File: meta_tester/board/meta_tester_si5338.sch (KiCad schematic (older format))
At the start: 0 parts

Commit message: Adding OPAMP
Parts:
- added C? (x4): CAP_0603, SM0603, symbol CAP_0603
- added C? (x4): CAP_0805, SM0805, symbol CAP_0805
- added P?: USB_OTG, symbol USB_OTG
- added U? (x2): TCA0372BDW-SOIC16, symbol TCA0372BDW-SOIC16
- added U?: MAX5713/4/5-TSSOP14, symbol MAX5713/4/5-TSSOP14
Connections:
- net labels added: +3.3V, +5V, CLR_DAC, CS_DAC, DAC0, DAC1, DAC2, DAC3, GND, MOSI_DAC, SCK_DAC, VddO0, VddO1, VddO2, VddO3
- wire segments 0 -> 85
- no-connect marks 0 -> 3

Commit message: starting layout
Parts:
- removed P?: USB_OTG, symbol USB_OTG
- added C101, C102: 100n, General_SMD:SM0805, symbol CAP_0805
- added C103, C107, C117, C118: 10p, General_SMD:SM0603, symbol CAP_0603
- added C113, C114, C115, C116, C120, C123, C130: 1u, General_SMD:SM0805, symbol CAP_0805
- added C119, C122, C125, C127: CAP_0603, General_SMD:SM0603, symbol CAP_0603
- added C121, C124, C126, C129: CAP_0805, General_SMD:SM0805, symbol CAP_0805
- added C128: 10n, General_SMD:SM0603, symbol CAP_0603
- added J101, J102, J103, J104, J105, J106, J107, J108: SMA_PCB, Connectors_RF:Border_Antenna, symbol SMA_PCB
- added L101, L102, L103: IND_0603, General_SMD:SM0603, symbol IND_0603
- added P101: USB_OTG, Connectors:USB_Mini-B, symbol USB_OTG
- added R101, R102, R103, R104: 1M, General_SMD:SM0603, symbol RES_0603
- added U103: STM32F103TB-QFN36, QFN:QFN36_6x6_0.5mm, symbol STM32F103TB-QFN36
- added U105: CH340T-SSOP20, SSOP:SSOP-20, symbol CH340T-SSOP20
- added U106: REG113-XX-SOT23, SOT:SOT-236-095mm, symbol REG113-XX-SOT23
- added X101: 8MHz, Xtal_SMD:xtal_3.2x2.5, symbol SMD_XTAL_small
- added X102: 12MHz, Xtal_SMD:xtal_3.2x2.5, symbol SMD_XTAL_small
- C104, C106, C109, C111: renamed from C?; footprint SM0603 -> General_SMD:SM0603
- C105, C108, C110, C112: renamed from C?; footprint SM0805 -> General_SMD:SM0805
- U101: renamed from U?; footprint (none) -> SSOP:SSOP14
- U102, U104: renamed from U?; footprint (none) -> SOIC:SOIC-16-10.3x7.5
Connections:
- net labels added: 5338_INT, D_N, D_P, PSU01, PSU23, SCL, SDA, US1_CTS, US1_RTS, US1_RX, US1_TX
- wire segments 85 -> 240
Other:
- note added: "3.3V"

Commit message: reversed CTS/RTS
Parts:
- P101: symbol USB_OTG -> USB_OTG-RESCUE-meta_tester_si5338
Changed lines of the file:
@@
 $EndComp
 $Comp
-L USB_OTG P101
+L USB_OTG-RESCUE-meta_tester_si5338 P101
 U 1 1 58AEF4E6
 P 8825 1450
@@
 Text Label 8125 1350 2    25   ~ 0
 US1_RX
+Text Label 7100 1700 0    25   ~ 0
+US1_RTS
 Text Label 7100 1450 0    25   ~ 0
-US1_RTS
-Text Label 7100 1700 0    25   ~ 0
 US1_CTS
 Wire Wire Line

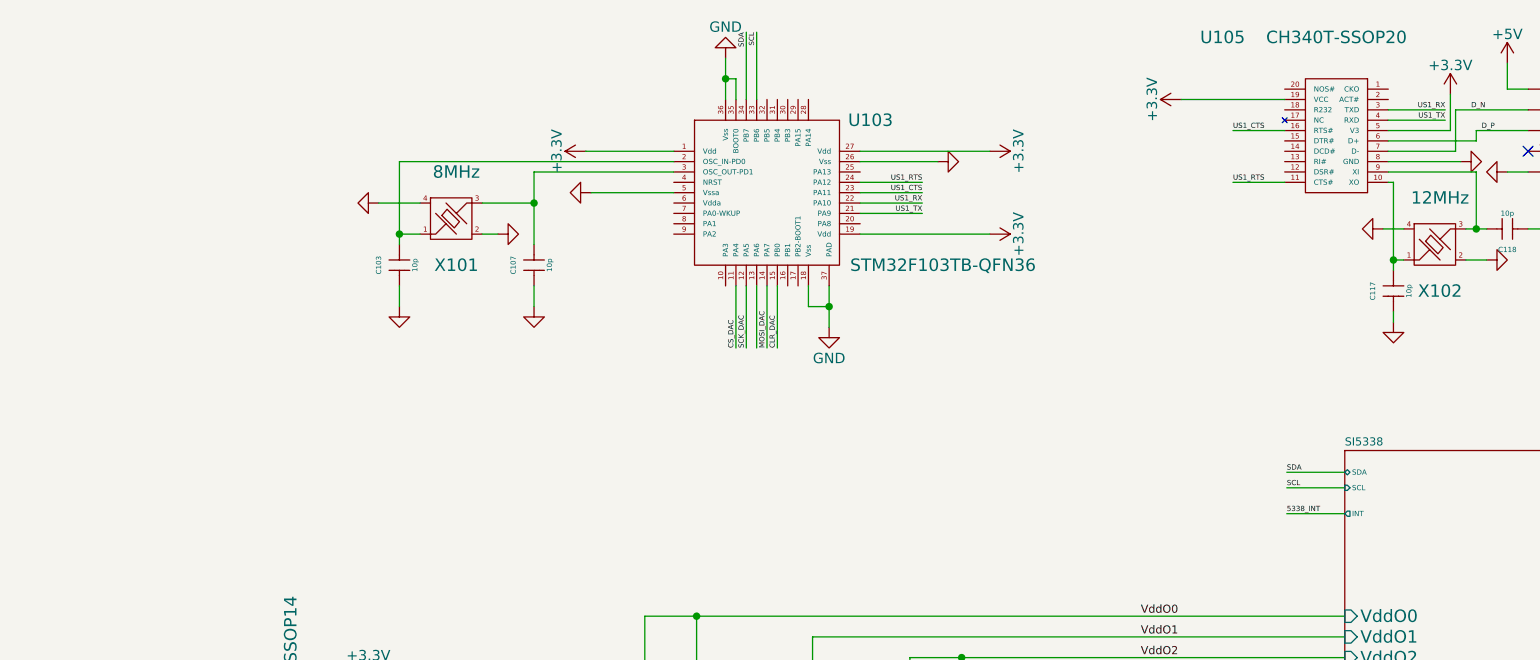
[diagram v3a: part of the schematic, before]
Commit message: adding jtag connector
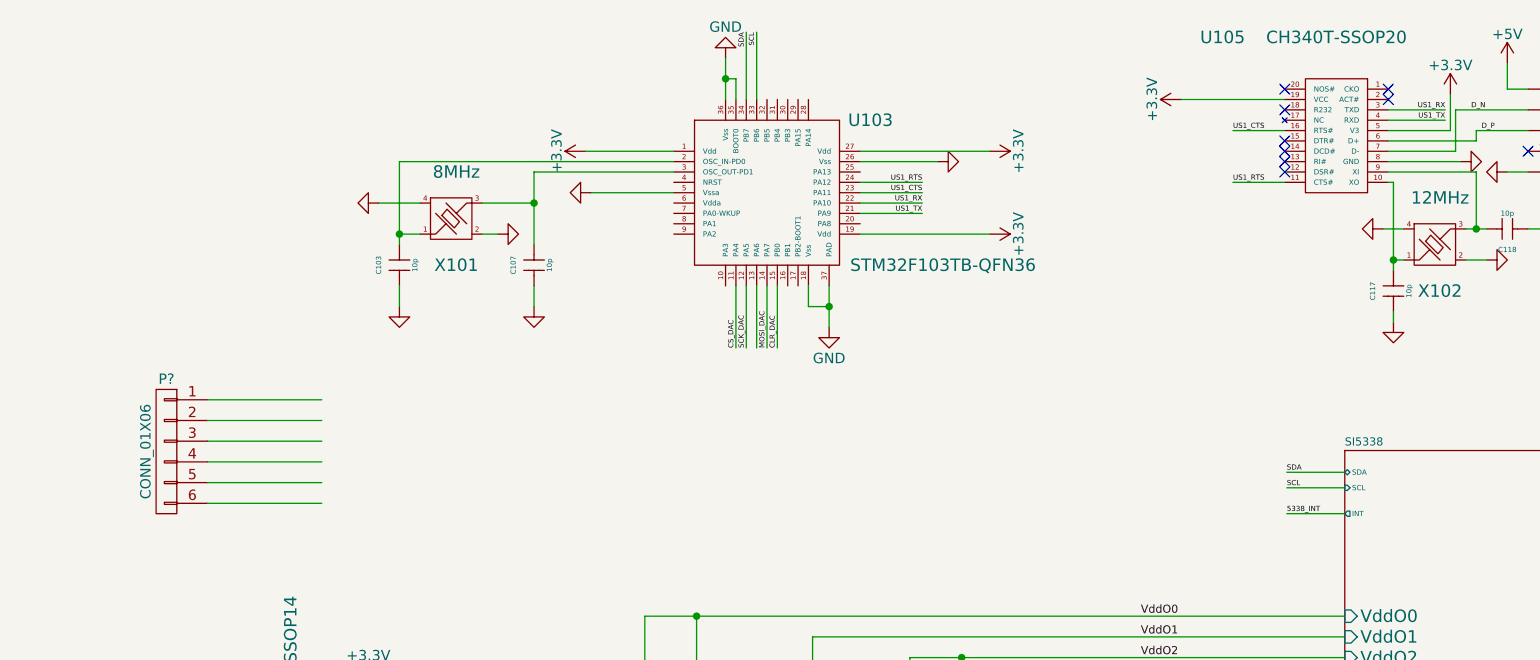
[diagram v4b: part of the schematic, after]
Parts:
- added P?: CONN_01X06, symbol CONN_01X06
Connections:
- no-connect marks 3 -> 11
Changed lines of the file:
@@
 	0    1    1    0
 $EndComp
+NoConn ~ 7850 1250
+NoConn ~ 7850 1300
+NoConn ~ 7350 1250
+NoConn ~ 7350 1350
+NoConn ~ 7350 1650
+NoConn ~ 7350 1600
+NoConn ~ 7350 1550
+NoConn ~ 7350 1500
+$Comp
+L CONN_01X06 P?
+U 1 1 58B060A0
+P 1950 3000
+F 0 "P?" H 1950 3350 50  0000 C CNN
+F 1 "CONN_01X06" V 2050 3000 50  0000 C CNN
+F 2 "" H 1950 3000 50  0000 C CNN
+F 3 "" H 1950 3000 50  0000 C CNN
+	1    1950 3000
+	-1   0    0    -1
+$EndComp
+Wire Wire Line
+	2150 2750 2700 2750
+Wire Wire Line
+	2150 2850 2700 2850
+Wire Wire Line
+	2150 2950 2700 2950
+Wire Wire Line
+	2150 3050 2700 3050
+Wire Wire Line
+	2150 3150 2700 3150
+Wire Wire Line
+	2150 3250 2700 3250
 $EndSCHEMATC

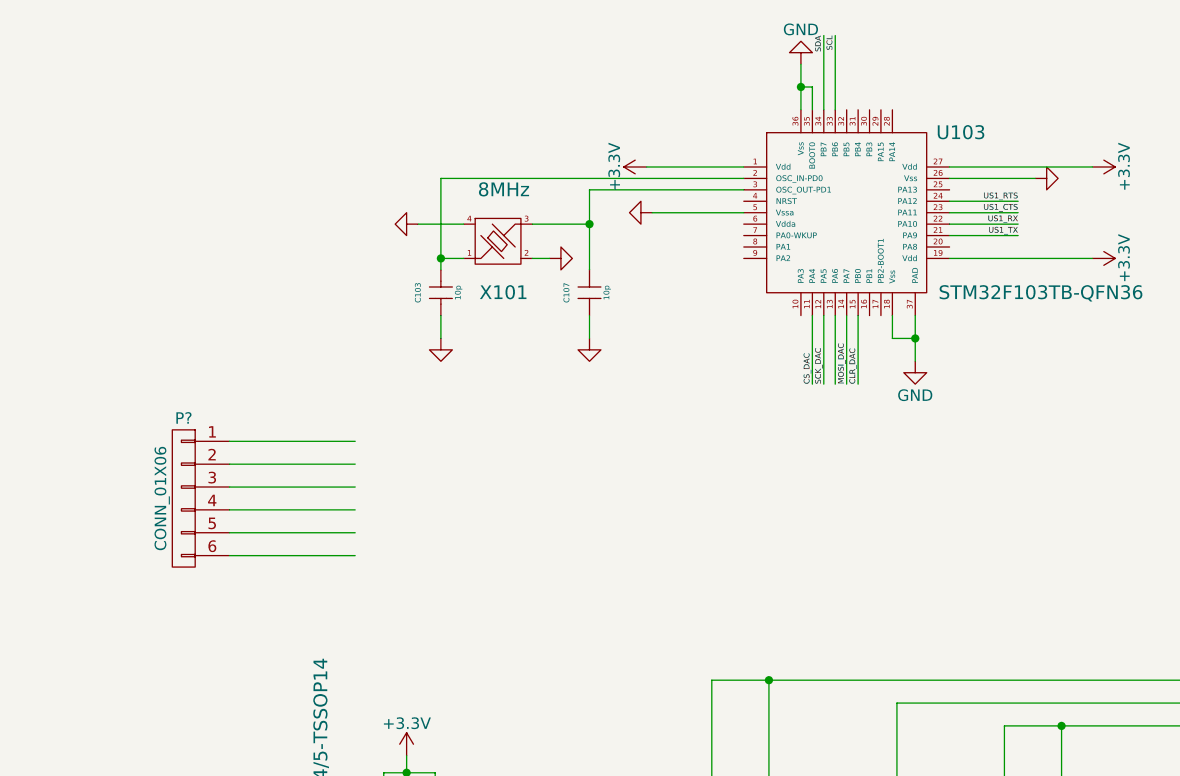
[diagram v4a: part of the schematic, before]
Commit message: starting placing components
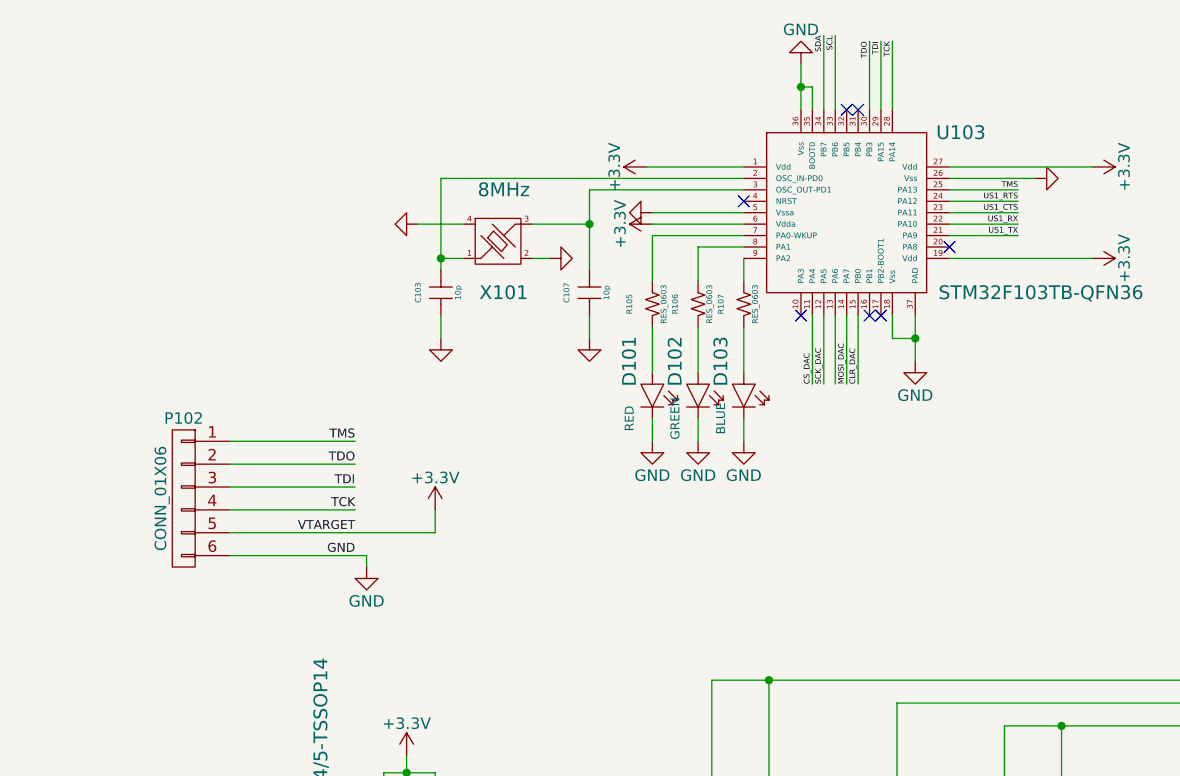
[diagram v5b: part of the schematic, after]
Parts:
- added D101: RED, General_SMD:LED-0603, symbol LED
- added D102: GREEN, General_SMD:LED-0603, symbol LED
- added D103: BLUE, General_SMD:LED-0603, symbol LED
- added R105, R106, R107: RES_0603, General_SMD:SM0603, symbol RES_0603
- P102: renamed from P?; footprint (none) -> Connectors_254mm:pin_array_6x1
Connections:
- net +3V3: now also P102.5 (P5), U103.6 (Vdda)
- net GND: now also P102.6 (P6), D101.K, D102.K, D103.K
- net TMS: now reaches U103.25 (PA13)
- net TMS: now also P102.1 (P1)
- net TCK: now reaches U103.28 (PA14)
- net TCK: now also P102.4 (P4)
- net TDI: now reaches U103.29 (PA15)
- net TDI: now also P102.3 (P3)
- net TDO: now reaches U103.30 (PB3)
- net TDO: now also P102.2 (P2)
- net at U103.7 (PA0-WKUP): now also R105.1
- net at U103.8 (PA1): now also R106.1
- net at U103.9 (PA2): now also R107.1
- new net: D101.A, R105.2
- new net: D102.A, R106.2
- new net: D103.A, R107.2
- no-connect marks 11 -> 18
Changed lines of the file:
@@
 LIBS:meta_tester_si5338-rescue
 LIBS:power
-LIBS:device
 LIBS:transistors
 LIBS:conn
@@
 NoConn ~ 7350 1500
 $Comp
-L CONN_01X06 P?
+L CONN_01X06 P102
 U 1 1 58B060A0
 P 1950 3000
-F 0 "P?" H 1950 3350 50  0000 C CNN
+F 0 "P102" H 1950 3350 50  0000 C CNN
 F 1 "CONN_01X06" V 2050 3000 50  0000 C CNN
-F 2 "" H 1950 3000 50  0000 C CNN
+F 2 "Connectors_254mm:pin_array_6x1" H 1950 3000 50  0001 C CNN
 F 3 "" H 1950 3000 50  0000 C CNN
 	1    1950 3000
@@
 	2150 3050 2700 3050
 Wire Wire Line
-	2150 3150 2700 3150
-Wire Wire Line
-	2150 3250 2700 3250
+	2150 3150 3050 3150
+Wire Wire Line
+	2150 3250 2750 3250
+Text Label 2700 2750 2    39   ~ 0
+TMS
+Text Label 2700 2850 2    39   ~ 0
+TDO
+Text Label 2700 2950 2    39   ~ 0
+TDI
+Text Label 2700 3050 2    39   ~ 0
+TCK
+Text Label 2700 3150 2    39   ~ 0
+VTARGET
+Text Label 2700 3250 2    39   ~ 0
+GND
+$Comp
+L +3.3V #PWR048
+U 1 1 58AFFA49
+P 3050 3050
+F 0 "#PWR048" H 3050 2900 50  0001 C CNN
+F 1 "+3.3V" H 3050 3190 50  0000 C CNN
+F 2 "" H 3050 3050 50  0000 C CNN
+F 3 "" H 3050 3050 50  0000 C CNN
+	1    3050 3050
+	1    0    0    -1
+$EndComp
+Wire Wire Line
+	3050 3150 3050 3050
+$Comp
+L GND #PWR049
+U 1 1 58B00265
+P 2750 3300
+F 0 "#PWR049" H 2750 3050 50  0001 C CNN
+F 1 "GND" H 2750 3150 50  0000 C CNN
+F 2 "" H 2750 3300 50  0000 C CNN
+F 3 "" H 2750 3300 50  0000 C CNN
+	1    2750 3300
+	1    0    0    -1
+$EndComp
+Wire Wire Line
+	2750 3250 2750 3300
+Wire Wire Line
+	5300 1650 5600 1650
+Text Label 5600 1650 2    25   ~ 0
+TMS
+Wire Wire Line
+	5050 1300 5050 1000
+Wire Wire Line
+	5000 1300 5000 1000
+Text Label 5050 1000 3    25   ~ 0
+TCK
+Text Label 5000 1000 3    25   ~ 0
+TDI
+Wire Wire Line
+	4950 1300 4950 1000
+Text Label 4950 1000 3    25   ~ 0
+TDO
+NoConn ~ 4400 1700
+Wire Wire Line
+	4400 1800 4000 1800
+$Comp
+L +3.3V #PWR050
+U 1 1 58B0377D
+P 4000 1800
+F 0 "#PWR050" H 4000 1650 50  0001 C CNN
+F 1 "+3.3V" H 4000 1940 50  0000 C CNN
+F 2 "" H 4000 1800 50  0000 C CNN
+F 3 "" H 4000 1800 50  0000 C CNN
+	1    4000 1800
+	0    -1   -1   0
+$EndComp
+$Comp
+L RES_0603 R105
+U 1 1 58B04926
+P 4000 2150
+F 0 "R105" H 4000 2050 25  0000 C CNN
+F 1 "RES_0603" H 4000 2200 25  0000 C CNN
+F 2 "General_SMD:SM0603" H 4000 2150 60  0001 C CNN
+F 3 "" H 4000 2150 60  0000 C CNN
+	1    4000 2150
+	0    1    1    0
+$EndComp
+$Comp
+L RES_0603 R106
+U 1 1 58B04A39
+P 4200 2150
+F 0 "R106" H 4200 2050 25  0000 C CNN
+F 1 "RES_0603" H 4200 2200 25  0000 C CNN
+F 2 "General_SMD:SM0603" H 4200 2150 60  0001 C CNN
+F 3 "" H 4200 2150 60  0000 C CNN
+	1    4200 2150
+	0    1    1    0
+$EndComp
+$Comp
+L RES_0603 R107
+U 1 1 58B04B22
+P 4400 2150
+F 0 "R107" H 4400 2050 25  0000 C CNN
+F 1 "RES_0603" H 4400 2200 25  0000 C CNN
+F 2 "General_SMD:SM0603" H 4400 2150 60  0001 C CNN
+F 3 "" H 4400 2150 60  0000 C CNN
+	1    4400 2150
+	0    1    1    0
+$EndComp
+Wire Wire Line
+	4400 1850 4000 1850
+Wire Wire Line
+	4000 1850 4000 2050
+Wire Wire Line
+	4400 1900 4200 1900
+Wire Wire Line
+	4200 1900 4200 2050
+Wire Wire Line
+	4400 1950 4400 2050
+Wire Wire Line
+	4400 2250 4400 2450
+Wire Wire Line
+	4200 2250 4200 2450
+Wire Wire Line
+	4000 2250 4000 2450
+$Comp
+L GND #PWR051
+U 1 1 58B05743
+P 4000 2750
+F 0 "#PWR051" H 4000 2500 50  0001 C CNN
+F 1 "GND" H 4000 2600 50  0000 C CNN
+F 2 "" H 4000 2750 50  0000 C CNN
+F 3 "" H 4000 2750 50  0000 C CNN
+	1    4000 2750
+	1    0    0    -1
+$EndComp
+$Comp
+L GND #PWR052
+U 1 1 58B0585F
+P 4200 2750
+F 0 "#PWR052" H 4200 2500 50  0001 C CNN
+F 1 "GND" H 4200 2600 50  0000 C CNN
+F 2 "" H 4200 2750 50  0000 C CNN
+F 3 "" H 4200 2750 50  0000 C CNN
+	1    4200 2750
+	1    0    0    -1
+$EndComp
+$Comp
+L GND #PWR053
+U 1 1 58B0597B
+P 4400 2750
+F 0 "#PWR053" H 4400 2500 50  0001 C CNN
+F 1 "GND" H 4400 2600 50  0000 C CNN
+F 2 "" H 4400 2750 50  0000 C CNN
+F 3 "" H 4400 2750 50  0000 C CNN
+	1    4400 2750
+	1    0    0    -1
+$EndComp
+Wire Wire Line
+	4400 2650 4400 2750
+Wire Wire Line
+	4200 2650 4200 2750
+Wire Wire Line
+	4000 2650 4000 2750
+NoConn ~ 4850 1300
+NoConn ~ 4900 1300
+NoConn ~ 4650 2200
+NoConn ~ 4950 2200
+NoConn ~ 5000 2200
+NoConn ~ 5300 1900
+$Comp
+L LED D101
+U 1 1 58AFF4F4
+P 4000 2550
+F 0 "D101" H 3850 2450 60  0000 C CNN
+F 1 "RED" H 4100 2450 39  0000 C CNN
+F 2 "General_SMD:LED-0603" H 4000 2550 60  0001 C CNN
+F 3 "" H 4000 2550 60  0000 C CNN
+	1    4000 2550
+	0    1    1    0
+$EndComp
+$Comp
+L LED D102
+U 1 1 58AFF5E5
+P 4200 2550
+F 0 "D102" H 4050 2450 60  0000 C CNN
+F 1 "GREEN" H 4300 2450 39  0000 C CNN
+F 2 "General_SMD:LED-0603" H 4200 2550 60  0001 C CNN
+F 3 "" H 4200 2550 60  0000 C CNN
+	1    4200 2550
+	0    1    1    0
+$EndComp
+$Comp
+L LED D103
+U 1 1 58AFF6CE
+P 4400 2550
+F 0 "D103" H 4250 2450 60  0000 C CNN
+F 1 "BLUE" H 4500 2450 39  0000 C CNN
+F 2 "General_SMD:LED-0603" H 4400 2550 60  0001 C CNN
+F 3 "" H 4400 2550 60  0000 C CNN
+	1    4400 2550
+	0    1    1    0
+$EndComp
 $EndSCHEMATC
